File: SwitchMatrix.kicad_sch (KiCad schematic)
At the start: 154 parts, among them SW1 1u, SW10 1u, SW11 1u, SW12 1u, SW13 1u, SW14 1u, SW15 1u, SW16 1u, SW17 2u, SW18 1.5u, SW19 1u, SW2 1u, SW20 1u, SW21 1u, SW22 1u, SW23 1u, SW24 1u, SW25 1u, SW26 1u, SW27 1u, SW28 1u, SW29 1u, SW3 1u, SW30 1u, SW31 1.5u, SW32 ISO Enter, SW33 1u, SW34 1.25u, SW35 1.75u, SW36 1u, SW37 1u, SW38 1u, SW39 1u, SW4 1u, SW40 1u, SW41 1u, SW42 1u, SW43 1u, SW44 1u, SW45 1u, SW46 1u, SW47 2.25u, SW48 1u, SW49 1u, SW5 1u, SW50 2.25u, SW51 1.25u, SW52 1u, SW53 1u, SW54 1u, SW55 1u, SW56 1u, SW57 1u, SW58 1u, SW59 1u, SW6 1u, SW60 1u, SW61 1u, SW62 1u, SW63 1u, SW64 1u, SW65 1u, SW66 1.5u, SW67 1u, SW68 1.5u, SW69 7u, SW7 1u, SW70 1.25u, SW71 1.5u, SW72 1u, SW73 1u, SW74 1u, SW75 1.25u, SW76 1.25u, SW77 1.25u, SW78 6.25u, SW79 1.25u, SW8 1u, SW81 3u, SW82 1u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

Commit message: idek
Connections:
- net ROW4: no longer D71.1 (K)
- net at D64.2 (A), SW69.2, SW78.2: now also D71.1 (K)
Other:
- moved on the sheet: D70, D72, SW81, SW83
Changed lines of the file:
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@@
   (junction (at 251.46 109.22) (diameter 0) (color 0 0 0 0)
   )
+  (junction (at 139.7 109.22) (diameter 0) (color 0 0 0 0)
+  )
   (junction (at 74.93 119.38) (diameter 0) (color 0 0 0 0)
   )
@@
   (junction (at 228.6 63.5) (diameter 0) (color 0 0 0 0)
   )
-  (junction (at 139.7 109.22) (diameter 0) (color 0 0 0 0)
-  )
   (junction (at 195.58 53.34) (diameter 0) (color 0 0 0 0)
   )
-  (junction (at 120.65 138.43) (diameter 0) (color 0 0 0 0)
-  )
   (junction (at 83.82 53.34) (diameter 0) (color 0 0 0 0)
   )
@@
   (junction (at 83.82 90.17) (diameter 0) (color 0 0 0 0)
   )
-  (junction (at 158.75 138.43) (diameter 0) (color 0 0 0 0)
-  )
   (junction (at 251.46 72.39) (diameter 0) (color 0 0 0 0)
   )
@@
   (junction (at 181.61 72.39) (diameter 0) (color 0 0 0 0)
   )
+  (junction (at 116.84 138.43) (diameter 0) (color 0 0 0 0)
+  )
   (junction (at 139.7 72.39) (diameter 0) (color 0 0 0 0)
   )
@@
   (junction (at 139.7 53.34) (diameter 0) (color 0 0 0 0)
   )
+  (junction (at 134.62 152.4) (diameter 0) (color 0 0 0 0)
+  )
   (junction (at 200.66 133.35) (diameter 0) (color 0 0 0 0)
   )
@@
     (stroke (width 0) (type default) (color 0 0 0 0))
   )
+  (wire (pts (xy 116.84 138.43) (xy 130.81 138.43))
+    (stroke (width 0) (type default) (color 0 0 0 0))
+  )
   (wire (pts (xy 55.88 53.34) (xy 55.88 72.39))
     (stroke (width 0) (type default) (color 0 0 0 0))
@@
     (stroke (width 0) (type default) (color 0 0 0 0))
   )
+  (wire (pts (xy 139.7 109.22) (xy 139.7 128.27))
+    (stroke (width 0) (type default) (color 0 0 0 0))
+  )
   (wire (pts (xy 125.73 128.27) (xy 125.73 147.32))
     (stroke (width 0) (type default) (color 0 0 0 0))
@@
     (stroke (width 0) (type default) (color 0 0 0 0))
   )
+  (wire (pts (xy 134.62 172.085) (xy 134.62 152.4))
+    (stroke (width 0) (type default) (color 0 0 0 0))
+  )
   (wire (pts (xy 102.87 100.33) (xy 116.84 100.33))
     (stroke (width 0) (type default) (color 0 0 0 0))
@@
     (stroke (width 0) (type default) (color 0 0 0 0))
   )
-  (wire (pts (xy 120.65 138.43) (xy 130.81 138.43))
-    (stroke (width 0) (type default) (color 0 0 0 0))
-  )
   (wire (pts (xy 116.84 63.5) (xy 130.81 63.5))
     (stroke (width 0) (type default) (color 0 0 0 0))
@@
     (stroke (width 0) (type default) (color 0 0 0 0))
   )
-  (wire (pts (xy 158.75 138.43) (xy 172.72 138.43))
+  (wire (pts (xy 144.78 138.43) (xy 172.72 138.43))
     (stroke (width 0) (type default) (color 0 0 0 0))
   )
@@
     (stroke (width 0) (type default) (color 0 0 0 0))
   )
-  (wire (pts (xy 130.81 172.085) (xy 130.81 175.895))
-    (stroke (width 0) (type default) (color 0 0 0 0))
-  )
   (wire (pts (xy 181.61 72.39) (xy 181.61 90.17))
     (stroke (width 0) (type default) (color 0 0 0 0))
@@
     (stroke (width 0) (type default) (color 0 0 0 0))
   )
+  (wire (pts (xy 130.81 172.085) (xy 134.62 172.085))
+    (stroke (width 0) (type default) (color 0 0 0 0))
+  )
   (wire (pts (xy 26.67 101.6) (xy 41.91 101.6))
     (stroke (width 0) (type default) (color 0 0 0 0))
@@
     (stroke (width 0) (type default) (color 0 0 0 0))
   )
-  (wire (pts (xy 147.955 139.7) (xy 144.78 139.7))
-    (stroke (width 0) (type default) (color 0 0 0 0))
-  )
   (wire (pts (xy 144.78 63.5) (xy 158.75 63.5))
     (stroke (width 0) (type default) (color 0 0 0 0))
@@
     (stroke (width 0) (type default) (color 0 0 0 0))
   )
-  (wire (pts (xy 139.7 109.22) (xy 139.7 161.925))
-    (stroke (width 0) (type default) (color 0 0 0 0))
-  )
   (wire (pts (xy 125.73 72.39) (xy 125.73 90.17))
     (stroke (width 0) (type default) (color 0 0 0 0))
@@
     (stroke (width 0) (type default) (color 0 0 0 0))
   )
-  (wire (pts (xy 144.78 172.085) (xy 147.955 172.085))
-    (stroke (width 0) (type default) (color 0 0 0 0))
-  )
   (wire (pts (xy 49.53 152.4) (xy 49.53 133.35))
     (stroke (width 0) (type default) (color 0 0 0 0))
@@
     (stroke (width 0) (type default) (color 0 0 0 0))
   )
-  (wire (pts (xy 144.78 138.43) (xy 158.75 138.43))
-    (stroke (width 0) (type default) (color 0 0 0 0))
-  )
-  (wire (pts (xy 147.955 172.085) (xy 147.955 139.7))
-    (stroke (width 0) (type default) (color 0 0 0 0))
-  )
   (wire (pts (xy 55.88 128.27) (xy 55.88 147.32))
     (stroke (width 0) (type default) (color 0 0 0 0))
@@
     (stroke (width 0) (type default) (color 0 0 0 0))
   )
-  (wire (pts (xy 158.75 175.895) (xy 158.75 138.43))
-    (stroke (width 0) (type default) (color 0 0 0 0))
-  )
   (wire (pts (xy 242.57 95.25) (xy 232.41 95.25))
     (stroke (width 0) (type default) (color 0 0 0 0))
@@
     (stroke (width 0) (type default) (color 0 0 0 0))
   )
-  (wire (pts (xy 120.65 172.085) (xy 120.65 138.43))
-    (stroke (width 0) (type default) (color 0 0 0 0))
-  )
   (wire (pts (xy 41.91 83.82) (xy 41.91 90.17))
     (stroke (width 0) (type default) (color 0 0 0 0))
@@
     (stroke (width 0) (type default) (color 0 0 0 0))
   )
-  (wire (pts (xy 130.81 175.895) (xy 158.75 175.895))
-    (stroke (width 0) (type default) (color 0 0 0 0))
-  )
-  (wire (pts (xy 111.76 109.22) (xy 111.76 161.925))
-    (stroke (width 0) (type default) (color 0 0 0 0))
-  )
-  (wire (pts (xy 116.84 172.085) (xy 120.65 172.085))
+  (wire (pts (xy 111.76 109.22) (xy 111.76 128.27))
     (stroke (width 0) (type default) (color 0 0 0 0))
   )
@@
     (stroke (width 0) (type default) (color 0 0 0 0))
   )
-  (wire (pts (xy 74.93 138.43) (xy 120.65 138.43))
+  (wire (pts (xy 74.93 138.43) (xy 116.84 138.43))
     (stroke (width 0) (type default) (color 0 0 0 0))
   )
@@
     (pin "2")
   )
-  (symbol (lib_id "marbastlib-mx:MX_SW_solder") (at 114.3 164.465 0) (unit 1)
-    (in_bom yes) (on_board yes) (fields_autoplaced)
-    (property "Reference" "SW81" (id 0) (at 114.3 156.21 0))
-    (property "Value" "3u" (id 1) (at 114.3 158.75 0))
-    (property "Footprint" "marbastlib-mx:SW_MX_1u" (id 2) (at 114.3 164.465 0)
-      (effects (font (size 1.27 1.27)) hide)
-    )
-    (property "Datasheet" "~" (id 3) (at 114.3 164.465 0)
+  (symbol (lib_id "marbastlib-mx:MX_SW_solder") (at 114.3 130.81 0) (unit 1)
+    (in_bom yes) (on_board yes) (fields_autoplaced)
+    (property "Reference" "SW81" (id 0) (at 114.3 122.555 0))
+    (property "Value" "3u" (id 1) (at 114.3 125.095 0))
+    (property "Footprint" "marbastlib-mx:SW_MX_1u" (id 2) (at 114.3 130.81 0)
+      (effects (font (size 1.27 1.27)) hide)
+    )
+    (property "Datasheet" "~" (id 3) (at 114.3 130.81 0)
       (effects (font (size 1.27 1.27)) hide)
     )
@@
     (pin "2")
   )
-  (symbol (lib_id "Device:D_Small") (at 116.84 169.545 90) (unit 1)
-    (in_bom yes) (on_board yes)
-    (property "Reference" "D70" (id 0) (at 109.22 169.545 0)
-      (effects (font (size 1.27 1.27)) (justify right))
-    )
-    (property "Value" "1N4148" (id 1) (at 109.22 160.655 0)
-      (effects (font (size 1.27 1.27)) (justify right))
-    )
-    (property "Footprint" "" (id 2) (at 116.84 169.545 90)
-      (effects (font (size 1.27 1.27)) hide)
-    )
-    (property "Datasheet" "~" (id 3) (at 116.84 169.545 90)
+  (symbol (lib_id "Device:D_Small") (at 116.84 135.89 90) (unit 1)
+    (in_bom yes) (on_board yes)
+    (property "Reference" "D70" (id 0) (at 109.22 134.62 0)
+      (effects (font (size 1.27 1.27)) (justify right))
+    )
+    (property "Value" "1N4148" (id 1) (at 109.22 125.73 0)
+      (effects (font (size 1.27 1.27)) (justify right))
+    )
+    (property "Footprint" "" (id 2) (at 116.84 135.89 90)
+      (effects (font (size 1.27 1.27)) hide)
+    )
+    (property "Datasheet" "~" (id 3) (at 116.84 135.89 90)
       (effects (font (size 1.27 1.27)) hide)
     )
@@
     (pin "2")
   )
-  (symbol (lib_id "Device:D_Small") (at 144.78 169.545 90) (unit 1)
-    (in_bom yes) (on_board yes)
-    (property "Reference" "D72" (id 0) (at 137.795 169.545 0)
-      (effects (font (size 1.27 1.27)) (justify right))
-    )
-    (property "Value" "1N4148" (id 1) (at 137.795 160.655 0)
-      (effects (font (size 1.27 1.27)) (justify right))
-    )
-    (property "Footprint" "" (id 2) (at 144.78 169.545 90)
-      (effects (font (size 1.27 1.27)) hide)
-    )
-    (property "Datasheet" "~" (id 3) (at 144.78 169.545 90)
+  (symbol (lib_id "Device:D_Small") (at 144.78 135.89 90) (unit 1)
+    (in_bom yes) (on_board yes)
+    (property "Reference" "D72" (id 0) (at 137.795 134.62 0)
+      (effects (font (size 1.27 1.27)) (justify right))
+    )
+    (property "Value" "1N4148" (id 1) (at 137.795 125.73 0)
+      (effects (font (size 1.27 1.27)) (justify right))
+    )
+    (property "Footprint" "" (id 2) (at 144.78 135.89 90)
+      (effects (font (size 1.27 1.27)) hide)
+    )
+    (property "Datasheet" "~" (id 3) (at 144.78 135.89 90)
       (effects (font (size 1.27 1.27)) hide)
     )
@@
     (pin "2")
   )
-  (symbol (lib_id "marbastlib-mx:MX_SW_solder") (at 142.24 164.465 0) (unit 1)
-    (in_bom yes) (on_board yes) (fields_autoplaced)
-    (property "Reference" "SW83" (id 0) (at 142.24 156.21 0))
-    (property "Value" "3u" (id 1) (at 142.24 158.75 0))
-    (property "Footprint" "marbastlib-mx:SW_MX_1u" (id 2) (at 142.24 164.465 0)
-      (effects (font (size 1.27 1.27)) hide)
-    )
-    (property "Datasheet" "~" (id 3) (at 142.24 164.465 0)
-      (effects (font (size 1.27 1.27)) hide)
-    )
+  (symbol (lib_id "marbastlib-mx:MX_SW_solder") (at 142.24 130.81 0) (unit 1)
+    (in_bom yes) (on_board yes) (fields_autoplaced)
+    (property "Reference" "SW83" (id 0) (at 142.24 122.555 0))
+    (property "Value" "3u" (id 1) (at 142.24 125.095 0))
+    (property "Footprint" "marbastlib-mx:SW_MX_1u" (id 2) (at 142.24 130.81 0)
+      (effects (font (size 1.27 1.27)) hide)
+    )
+    (property "Datasheet" "~" (id 3) (at 142.24 130.81 0)
+      (effects (font (size 1.27 1.27)) hide)
+    )

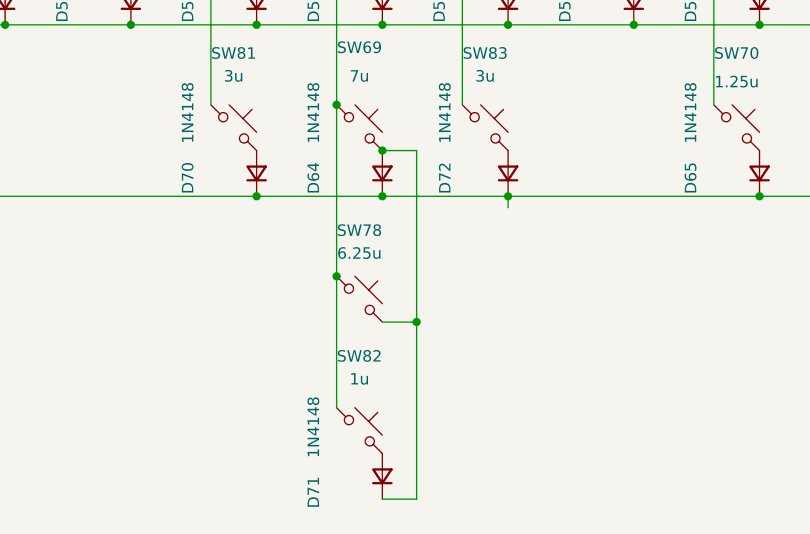
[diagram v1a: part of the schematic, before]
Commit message: Assign footprints
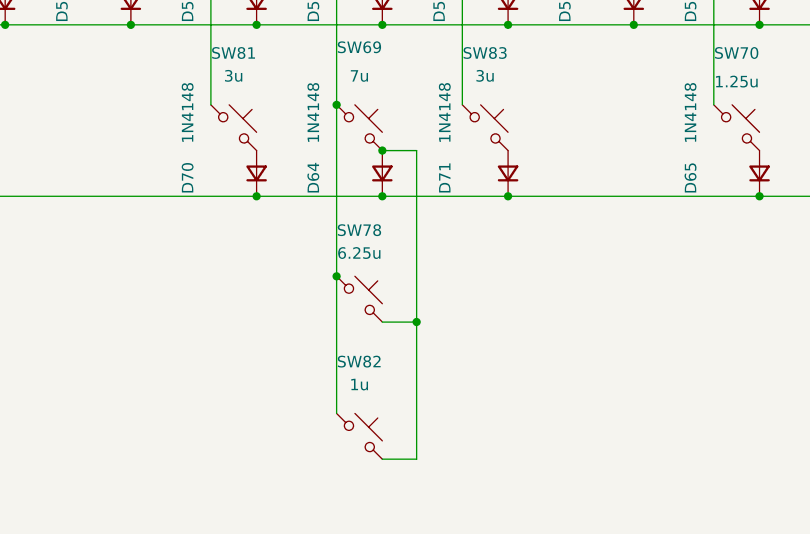
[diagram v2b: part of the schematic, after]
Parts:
- removed D71: 1N4148, symbol Device:D_Small
- D1, D10, D11, D12, D13, D14, D15, D16, D17, D18, D19, D2, D20, D21, D22, D23, D24, D25, D26, D27, D28, D29, D3, D30, D31, D32, D33, D34, D35, D36, D37, D38, D39, D4, D40, D41, D42, D43, D44, D45, D46, D47, D48, D49, D5, D50, D51, D52, D53, D54, D55, D56, D57, D58, D59, D6, D60, D61, D62, D63, D64, D65, D66, D67, D68, D69, D7, D70, D8, D9: footprint (none) -> Diode_SMD:D_SOD-123
- D71: renamed from D72; footprint (none) -> Diode_SMD:D_SOD-123
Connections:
- net at D64.2 (A), SW69.2, SW78.2: now also SW82.2
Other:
- moved on the sheet: SW82

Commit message: Add stabs
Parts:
- added S1, S2, S3, S4, S5, S6, S7: MX_stab, marbastlib-mx:STAB_MX_P_6.25u, symbol marbastlib-mx:MX_stab
- SW63: value 1u -> 1.75u
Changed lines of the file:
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@@
     (pin "2")
+  )
+  (symbol (lib_id "marbastlib-mx:MX_stab") (at 147.32 157.48 0) (unit 1)
+    (in_bom yes) (on_board yes) (fields_autoplaced)
+    (property "Reference" "S7" (id 0) (at 153.67 156.0829 0)
+      (effects (font (size 1.27 1.27)) (justify left))
+    )
+    (property "Value" "MX_stab" (id 1) (at 153.67 158.6229 0)
+      (effects (font (size 1.27 1.27)) (justify left))
+    )
+    (property "Footprint" "marbastlib-mx:STAB_MX_P_6.25u" (id 2) (at 147.32 157.48 0)
+      (effects (font (size 1.27 1.27)) hide)
+    )
+    (property "Datasheet" "" (id 3) (at 147.32 157.48 0)
+      (effects (font (size 1.27 1.27)) hide)
+    )
   )
   (symbol (lib_id "marbastlib-mx:MX_SW_solder") (at 226.06 74.93 0) (unit 1)
@@
     (pin "2")
   )
+  (symbol (lib_id "marbastlib-mx:MX_stab") (at 22.86 110.49 270) (unit 1)
+    (in_bom yes) (on_board yes)
+    (property "Reference" "S2" (id 0) (at 15.24 107.95 90)
+      (effects (font (size 1.27 1.27)) (justify left))
+    )
+    (property "Value" "MX_stab" (id 1) (at 12.7 110.49 90)
+      (effects (font (size 1.27 1.27)) (justify left))
+    )
+    (property "Footprint" "marbastlib-mx:STAB_MX_P_6.25u" (id 2) (at 22.86 110.49 0)
+      (effects (font (size 1.27 1.27)) hide)
+    )
+    (property "Datasheet" "" (id 3) (at 22.86 110.49 0)
+      (effects (font (size 1.27 1.27)) hide)
+    )
+  )
   (symbol (lib_id "Device:D_Small") (at 172.72 60.96 90) (unit 1)
     (in_bom yes) (on_board yes)
@@
     (pin "2")
   )
+  (symbol (lib_id "marbastlib-mx:MX_stab") (at 147.32 146.05 0) (unit 1)
+    (in_bom yes) (on_board yes) (fields_autoplaced)
+    (property "Reference" "S5" (id 0) (at 153.67 144.6529 0)
+      (effects (font (size 1.27 1.27)) (justify left))
+    )
+    (property "Value" "MX_stab" (id 1) (at 153.67 147.1929 0)
+      (effects (font (size 1.27 1.27)) (justify left))
+    )
+    (property "Footprint" "marbastlib-mx:STAB_MX_P_6.25u" (id 2) (at 147.32 146.05 0)
+      (effects (font (size 1.27 1.27)) hide)
+    )
+    (property "Datasheet" "" (id 3) (at 147.32 146.05 0)
+      (effects (font (size 1.27 1.27)) hide)
+    )
+  )
   (symbol (lib_id "Device:D_Small") (at 130.81 60.96 90) (unit 1)
     (in_bom yes) (on_board yes)
@@
     (pin "2")
   )
+  (symbol (lib_id "marbastlib-mx:MX_stab") (at 106.68 146.05 0) (unit 1)
+    (in_bom yes) (on_board yes) (fields_autoplaced)
+    (property "Reference" "S4" (id 0) (at 113.03 144.6529 0)
+      (effects (font (size 1.27 1.27)) (justify left))
+    )
+    (property "Value" "MX_stab" (id 1) (at 113.03 147.1929 0)
+      (effects (font (size 1.27 1.27)) (justify left))
+    )
+    (property "Footprint" "marbastlib-mx:STAB_MX_P_6.25u" (id 2) (at 106.68 146.05 0)
+      (effects (font (size 1.27 1.27)) hide)
+    )
+    (property "Datasheet" "" (id 3) (at 106.68 146.05 0)
+      (effects (font (size 1.27 1.27)) hide)
+    )
+  )
   (symbol (lib_id "marbastlib-mx:MX_SW_solder") (at 198.12 130.81 0) (unit 1)
     (in_bom yes) (on_board yes)
@@
     (pin "2")
   )
+  (symbol (lib_id "marbastlib-mx:MX_stab") (at 274.32 57.15 90) (unit 1)
+    (in_bom yes) (on_board yes)
+    (property "Reference" "S1" (id 0) (at 276.86 55.88 90)
+      (effects (font (size 1.27 1.27)) (justify right))
+    )
+    (property "Value" "MX_stab" (id 1) (at 276.86 58.42 90)
+      (effects (font (size 1.27 1.27)) (justify right))
+    )
+    (property "Footprint" "marbastlib-mx:STAB_MX_P_6.25u" (id 2) (at 274.32 57.15 0)
+      (effects (font (size 1.27 1.27)) hide)
+    )
+    (property "Datasheet" "" (id 3) (at 274.32 57.15 0)
+      (effects (font (size 1.27 1.27)) hide)
+    )
+  )
   (symbol (lib_id "Device:D_Small") (at 116.84 97.79 90) (unit 1)
     (in_bom yes) (on_board yes)
@@
     (pin "1")
     (pin "2")
+  )
+  (symbol (lib_id "marbastlib-mx:MX_stab") (at 265.43 74.93 90) (unit 1)
+    (in_bom yes) (on_board yes) (fields_autoplaced)
+    (property "Reference" "S3" (id 0) (at 269.24 73.6599 90)
+      (effects (font (size 1.27 1.27)) (justify right))
+    )
+    (property "Value" "MX_stab" (id 1) (at 269.24 76.1999 90)
+      (effects (font (size 1.27 1.27)) (justify right))
+    )
+    (property "Footprint" "marbastlib-mx:STAB_MX_P_6.25u" (id 2) (at 265.43 74.93 0)
+      (effects (font (size 1.27 1.27)) hide)
+    )
+    (property "Datasheet" "" (id 3) (at 265.43 74.93 0)
+      (effects (font (size 1.27 1.27)) hide)
+    )
   )
   (symbol (lib_id "marbastlib-mx:MX_SW_solder") (at 142.24 111.76 0) (unit 1)
@@
     (in_bom yes) (on_board yes) (fields_autoplaced)
     (property "Reference" "SW63" (id 0) (at 212.09 104.14 0))
-    (property "Value" "1u" (id 1) (at 212.09 106.68 0))
+    (property "Value" "1.75u" (id 1) (at 212.09 106.68 0))
     (property "Footprint" "marbastlib-mx:SW_MX_1u" (id 2) (at 212.09 111.76 0)
       (effects (font (size 1.27 1.27)) hide)
@@
     (pin "2")
   )
+  (symbol (lib_id "marbastlib-mx:MX_stab") (at 106.68 157.48 0) (unit 1)
+    (in_bom yes) (on_board yes) (fields_autoplaced)
+    (property "Reference" "S6" (id 0) (at 113.03 156.0829 0)
+      (effects (font (size 1.27 1.27)) (justify left))
+    )
+    (property "Value" "MX_stab" (id 1) (at 113.03 158.6229 0)
+      (effects (font (size 1.27 1.27)) (justify left))
+    )
+    (property "Footprint" "marbastlib-mx:STAB_MX_P_6.25u" (id 2) (at 106.68 157.48 0)
+      (effects (font (size 1.27 1.27)) hide)
+    )
+    (property "Datasheet" "" (id 3) (at 106.68 157.48 0)
+      (effects (font (size 1.27 1.27)) hide)
+    )
+  )
   (symbol (lib_id "marbastlib-mx:MX_SW_solder") (at 58.42 149.86 0) (unit 1)
